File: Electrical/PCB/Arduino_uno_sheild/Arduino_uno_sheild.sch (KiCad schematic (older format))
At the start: 15 parts, among them J1 ED10523-ND, J2 6posheader, J3 6posheader, J4 6posheader, J5 6posheader, J6 ED2580-ND

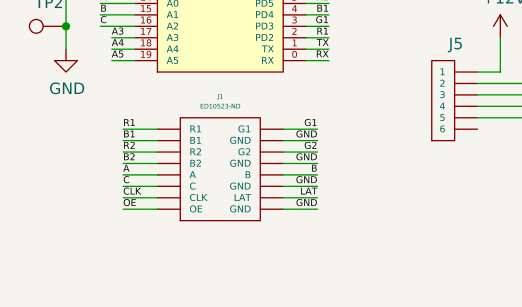
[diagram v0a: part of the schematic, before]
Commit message: Adding board Rev-E of control board with updated silkscreen images, and Rev-D of arduino board also with silk screen fixes
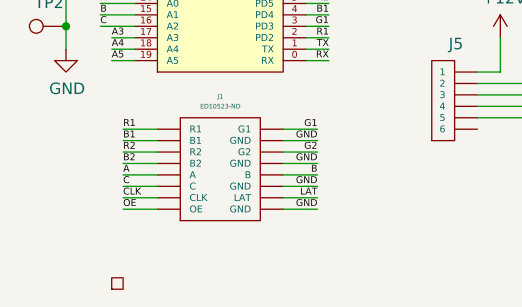
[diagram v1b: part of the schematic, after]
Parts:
- added y1: rover_silkscreen, JPL Robotics:rover_image, symbol Arduino_uno_sheild-rescue:rover_silkscreen
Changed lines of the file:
@@
 Connection ~ 5200 3200
 Connection ~ 4400 3150
+$Comp
+L Arduino_uno_sheild-rescue:rover_silkscreen y1
+U 1 1 5D3EF344
+P 2500 4050
+F 0 "y1" H 2578 4075 50  0001 L CNN
+F 1 "rover_silkscreen" H 2578 4030 50  0001 L CNN
+F 2 "JPL Robotics:rover_image" H 2500 4050 50  0001 C CNN
+F 3 "" H 2500 4050 50  0001 C CNN
+	1    2500 4050
+	1    0    0    -1
+$EndComp
 $EndSCHEMATC
